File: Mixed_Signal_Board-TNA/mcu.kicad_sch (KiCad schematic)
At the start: 40 parts, among them J200 USB_C_Receptacle_USB2.0_14P, J201 2x5 1.27mm, U200 STM32F103CBT6, U201 USBLC6-2SC6, Y200 16MHz

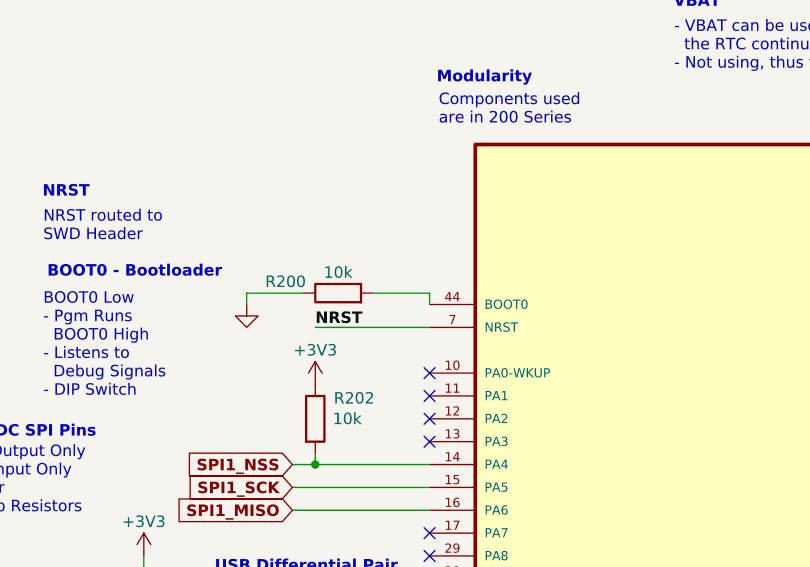
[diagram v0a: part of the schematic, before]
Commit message: Routed but differential pair not right
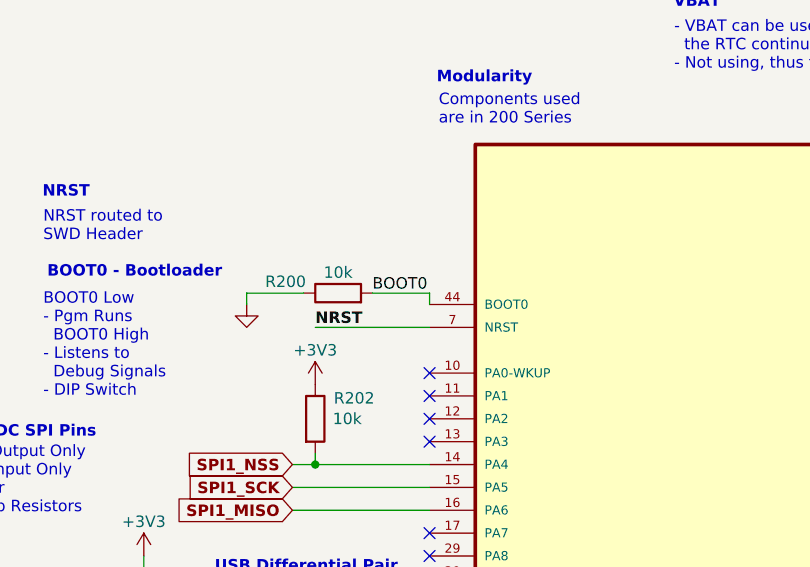
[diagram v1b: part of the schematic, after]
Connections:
- net BOOT0: now reaches R200.2, U200.44 (BOOT0)
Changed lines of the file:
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@@
+		)
+	)
+	(label "BOOT0"
+		(at 73.66 72.39 0)
+		(effects
+			(font
+				(size 1.27 1.27)
+			)
+			(justify left bottom)
 		)
 	)
